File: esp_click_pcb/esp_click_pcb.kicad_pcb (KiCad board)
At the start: 2 copper layers, 90 x 60 mm, 53 parts, among them J1 USB_C, SW1 BOOT, SW2 FLASH, SW3 BT1, SW4 BT2, SW5 BT3, SW6 BT4, U1 ESP32-C6-MINI, U2 HT7833, U4 BQ24075

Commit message: pcb layout complete
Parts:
- D1, D2, D3: footprint LED_SMD:LED_0201_0603Metric -> LED_SMD:LED_0603_1608Metric
- U4: value BQ24075 -> BQ24075RGT
- moved R16 162.6 mm to (183.0, 127.0)
- moved R4 153.1 mm to (172.0, 122.4), turned to 180 degrees
- moved R15 145.7 mm to (161.0, 127.0)
- moved R2 132.7 mm to (148.8, 116.9), turned to 90 degrees
- moved R5 131.7 mm to (151.2, 116.9), turned to 90 degrees
- moved R14 123.8 mm to (139.0, 127.0)
- moved R1 121.5 mm to (128.0, 122.4), turned to 180 degrees
- moved R13 109.1 mm to (117.0, 127.0)
- moved R11 102.3 mm to (130.7, 96.5)
- moved R18 100.7 mm to (117.6, 113.6)
- moved R10 99.8 mm to (126.5, 96.5)
- moved R17 99.3 mm to (113.8, 113.6), turned to 180 degrees
- moved R19 95.5 mm to (120.4, 104.5), turned to 90 degrees
- moved R3 91.9 mm to (124.0, 81.0), turned to 180 degrees
- moved C3 12.1 mm to (107.6, 93.2), turned to 180 degrees
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
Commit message: layout finished pcb
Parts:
- moved SW2 0.10 mm to (172.0, 127.5)
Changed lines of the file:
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@@
 	(footprint "TS-A002:TST-A002_0.6MM_BOSS"
 		(layer "F.Cu")
-		(at 128 127.5 180)
+		(at 128 127.55 180)
 		(property "Reference" "SW1"
 			(at 1 3 0)
@@
 	(footprint "TS-A002:TST-A002_0.6MM_BOSS"
 		(layer "F.Cu")
-		(at 172 127.45 180)
+		(at 172 127.55 180)
 		(property "Reference" "SW2"
 			(at 1 3 0)

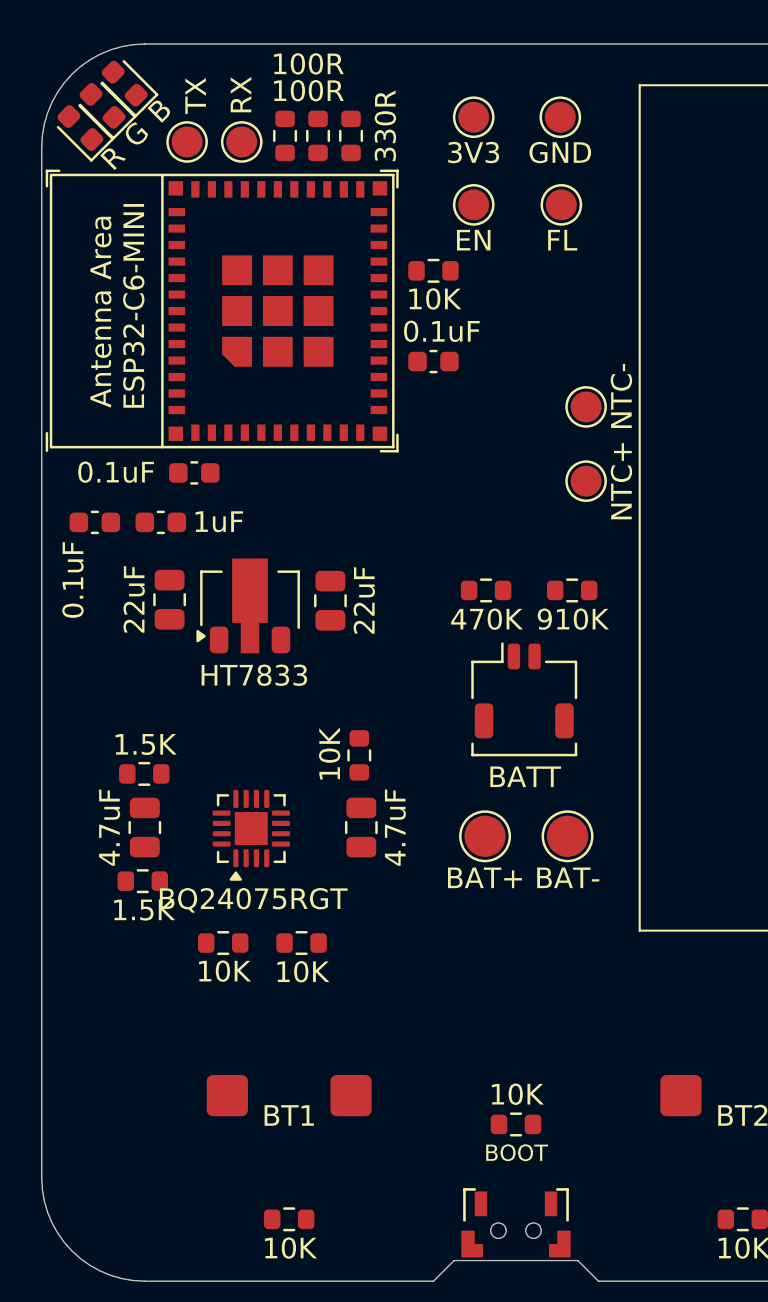
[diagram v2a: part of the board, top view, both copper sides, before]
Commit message: use rgb led directly
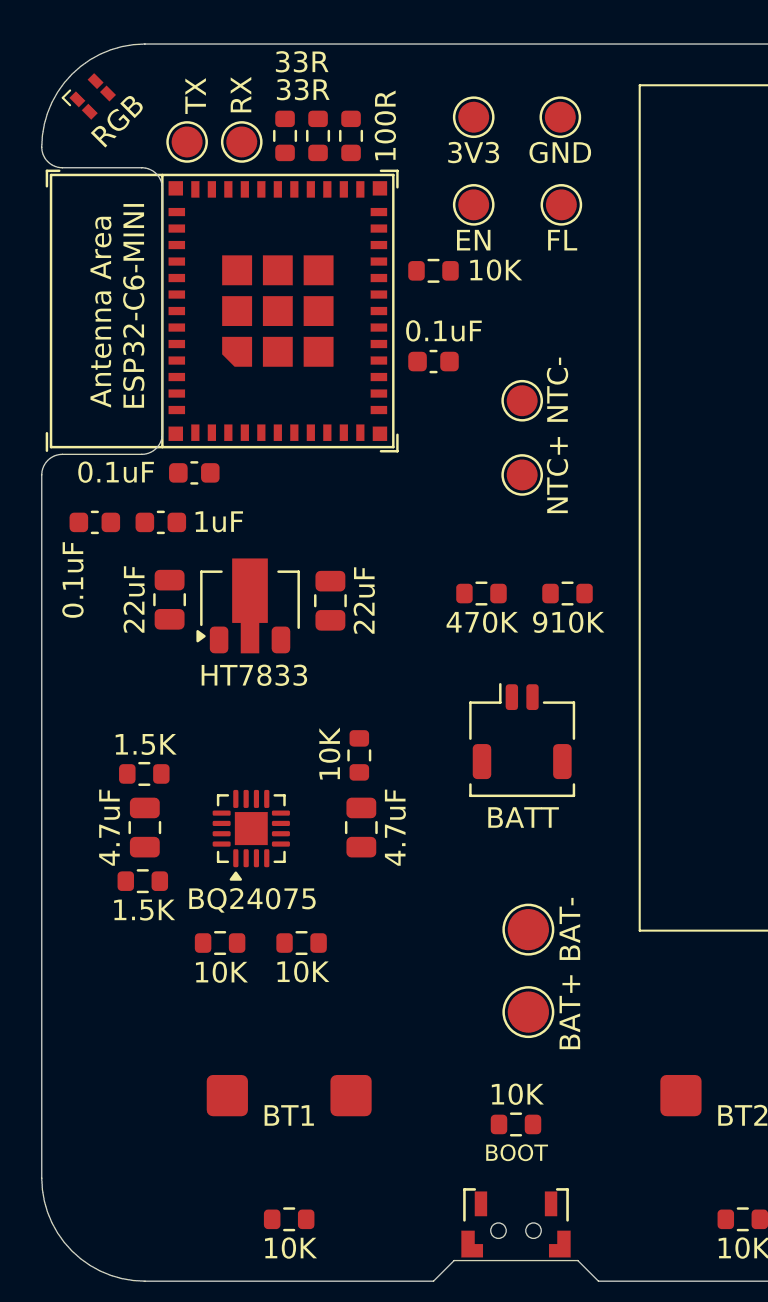
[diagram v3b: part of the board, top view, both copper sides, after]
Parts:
- removed D1: R, LED_SMD:LED_0603_1608Metric
- removed D2: G, LED_SMD:LED_0603_1608Metric
- removed D3: B, LED_SMD:LED_0603_1608Metric
- added LED1: RGB, XL-1615RGBC-RF:XL-1615RGBC-RF, F.Cu at (107.5, 72.5)
- R12, R21: value 100R -> 33R
- R20: value 330R -> 100R
- U4: value BQ24075RGT -> BQ24075
- moved TP7 8.78 mm to (128.6, 117.0), turned to 90 degrees
- moved TP8 4.91 mm to (128.6, 113.0), turned to 90 degrees
- moved TP10 3.11 mm to (128.3, 87.3)
- moved TP9 3.11 mm to (128.3, 90.9)
- moved BATT1 1.98 mm to (128.3, 103.3)
- moved R10 0.27 mm to (126.3, 96.7)
- moved R11 0.27 mm to (130.5, 96.7)
- moved R17 0.15 mm to (113.7, 113.6)
- turned R3 to 0 degrees
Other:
- outline, holes or cut-outs redrawn

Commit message: complete pcb design
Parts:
- moved C3 9.80 mm to (117.3, 92.2)
- moved C5 9.80 mm to (120.5, 92.2), turned to 0 degrees
- moved R2 3.20 mm to (152.0, 116.8)
- moved R5 3.20 mm to (148.0, 116.8)
- moved TP7 0.81 mm to (128.0, 117.5)
- moved TP8 0.81 mm to (128.0, 113.5)
- moved TP6 0.18 mm to (114.6, 74.6)
- moved TP5 0.18 mm to (112.0, 74.6)
- turned R12 to -90 degrees
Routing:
- net +3.3V: track 0.00 -> 197.2 mm, vias 0 -> 7
- net Net-(U1-EN/CHIP_PU): track 0.00 -> 109.3 mm, vias 0 -> 7
- net Net-(U1-GPIO9): track 0.00 -> 106.1 mm, vias 0 -> 4
- net B4: track 0.00 -> 99.3 mm, vias 0 -> 4
- net B3: track 0.00 -> 77.9 mm, vias 0 -> 4
- net +5V: track 0.00 -> 69.3 mm
- net B1: track 0.00 -> 63.6 mm, vias 0 -> 6
- net B2: track 0.00 -> 60.7 mm, vias 0 -> 6
- net Net-(U1-GPIO13/USB_D+): track 0.00 -> 59.7 mm
- net Net-(U1-GPIO12/USB_D-): track 0.00 -> 59.4 mm
- net GND: track 0.00 -> 42.9 mm, vias 0 -> 81
- net Net-(U4-TS): track 0.00 -> 42.7 mm, vias 0 -> 2
- net BATT+: track 0.00 -> 41.4 mm
- net CHG: track 0.00 -> 36.1 mm, vias 0 -> 2
- net PGOOD: track 0.00 -> 35.0 mm, vias 0 -> 4
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- added copper zone on B.Cu, net GND
- added copper zone on F.Cu, net GND
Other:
- outline, holes or cut-outs redrawn

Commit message: production build
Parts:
- added G***: LOGO, LOGO, F.Cu at (165.0, 87.0)
- added G***: LOGO, LOGO, B.Cu at (150.0, 94.0)
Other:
- board text added: "ESP CLICK"
- board text added: "JLCJLCJLCJLC"
- board text added: "REV 1 - 2026 MADHUKAR TEMBA"

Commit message: update pcb design, rev2
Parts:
- removed R4: 10K, Resistor_SMD:R_0603_1608Metric
- R12, R21: value 33R -> 100R
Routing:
- net +3.3V: track 197.2 -> 194.0 mm
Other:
- board text added: "REV 2 - 2026 MADHUKAR TEMBA"
- board text removed: "REV 1 - 2026 MADHUKAR TEMBA"
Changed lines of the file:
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@@
 	(title_block
 		(title "ESP Click")
-		(date "2026-03-06")
-		(rev "1")
+		(date "2026-03-13")
+		(rev "2")
 		(company "Madhukar Temba")
 	)
@@
 			)
 		)
-		(property "Value" "33R"
+		(property "Value" "100R"
 			(at -3.555 -0.8 180)
 			(layer "F.SilkS")
@@
 		(embedded_fonts no)
 	)
-	(footprint "Resistor_SMD:R_0603_1608Metric"
-		(layer "F.Cu")
-		(at 172 122.4 180)
-		(descr "Resistor SMD 0603 (1608 Metric), square (rectangular) end terminal, IPC-7351 nominal, (Body size source: IPC-SM-782 page 72, https://www.pcb-3d.com/wordpress/wp-content/uploads/ipc-sm-782a_amendment_1_and_2.pdf), generated with kicad-footprint-generator")
-		(tags "resistor")
-		(property "Reference" "R4"
-			(at 0 -1.43 0)
-			(layer "User.4")
-			(effects
-				(font
-					(size 1 1)
-					(thickness 0.15)
-				)
-			)
-		)
-		(property "Value" "10K"
-			(at 0 1.43 0)
-			(layer "F.SilkS")
-			(effects
-				(font
-					(size 1 1)
-					(thickness 0.15)
-				)
-			)
-		)
-		(property "Datasheet" "~"
-			(at 0 0 0)
-			(layer "F.Fab")
-			(hide yes)
-			(effects
-				(font
-					(size 1.27 1.27)
-					(thickness 0.15)
-				)
-			)
-		)
-		(property "Description" "Resistor"
-			(at 0 0 0)
-			(layer "F.Fab")
-			(hide yes)
-			(effects
-				(font
-					(size 1.27 1.27)
-					(thickness 0.15)
-				)
-			)
-		)
-		(property ki_fp_filters "R_*")
-		(sheetname "/")
-		(sheetfile "esp_click_pcb.kicad_sch")
-		(attr smd)
-		(fp_line
-			(start -0.237258 0.5225)
-			(end 0.237258 0.5225)
-			(stroke
-				(width 0.12)
-				(type solid)
-			)
-			(layer "F.SilkS")
-		)
-		(fp_line
-			(start -0.237258 -0.5225)
-			(end 0.237258 -0.5225)
-			(stroke
-				(width 0.12)
-				(type solid)
-			)
-			(layer "F.SilkS")
-		)
-		(fp_rect
-			(start -1.48 -0.73)
-			(end 1.48 0.73)
-			(stroke
-				(width 0.05)
-				(type solid)
-			)
-			(fill no)
-			(layer "F.CrtYd")
-		)
-		(fp_rect
-			(start -0.8 -0.4125)
-			(end 0.8 0.4125)
-			(stroke
-				(width 0.1)
-				(type solid)
-			)
-			(fill no)
-			(layer "F.Fab")
-		)
-		(fp_text user "${REFERENCE}"
-			(at 0 0 0)
-			(layer "User.4")
-			(effects
-				(font
-					(size 0.4 0.4)
-					(thickness 0.06)
-				)
-			)
-		)
-		(pad "1" smd roundrect
-			(at -0.825 0 180)
-			(size 0.8 0.95)
-			(layers "F.Cu" "F.Mask" "F.Paste")
-			(roundrect_rratio 0.25)
-			(net 16 "Net-(U1-GPIO9)")
-			(pintype "passive")
-		)
-		(pad "2" smd roundrect
-			(at 0.825 0 180)
-			(size 0.8 0.95)
-			(layers "F.Cu" "F.Mask" "F.Paste")
-			(roundrect_rratio 0.25)
-			(net 3 "+3.3V")
-			(pintype "passive")
-		)
-		(embedded_fonts no)
-		(model "${KICAD9_3DMODEL_DIR}/Resistor_SMD.3dshapes/R_0603_1608Metric.step"
-			(offset
-				(xyz 0 0 0)
-			)
-			(scale
-				(xyz 1 1 1)
-			)
-			(rotate
-				(xyz 0 0 0)
-			)
-		)
-	)
 	(footprint "TestPoint:TestPoint_Pad_D1.5mm"
 		(layer "F.Cu")
@@
 			)
 		)
-		(property "Value" "33R"
+		(property "Value" "100R"
 			(at -2.155 0.8 0)
 			(layer "F.SilkS")
@@
 		)
 	)
-	(gr_text "REV 1 - 2026\nMADHUKAR TEMBA"
+	(gr_text "REV 2 - 2026\nMADHUKAR TEMBA"
 		(at 189 125 0)
 		(layer "B.SilkS")
@@
 			(justify left bottom mirror)
 		)
-		(render_cache "REV 1 - 2026\nMADHUKAR TEMBA" 0
+		(render_cache "REV 2 - 2026\nMADHUKAR TEMBA" 0
 			(polygon
 				(pts
@@
 			(polygon
 				(pts
-					(xy 178.644347 119.45) (xy 178.644347 117.271598) (xy 179.19829 117.699694) (xy 179.563555 117.20034)
-					(xy 178.585546 116.483914) (xy 177.939279 116.483914) (xy 177.939279 119.45)
+					(xy 179.546702 119.45) (xy 179.546702 118.865465) (xy 178.388258 117.82151) (xy 178.287825 117.71381)
+					(xy 178.212037 117.608653) (xy 178.161801 117.494462) (xy 178.144809 117.366486) (xy 178.156618 117.264867)
+					(xy 178.190265 117.180568) (xy 178.24556 117.109665) (xy 178.318151 117.056213) (xy 178.406267 117.023193)
+					(xy 178.514288 117.011479) (xy 178.626245 117.025697) (xy 178.72064 117.066697) (xy 178.8017 117.13531)
+					(xy 178.864203 117.223546) (xy 178.908625 117.330616) (xy 178.933958 117.460642) (xy 179.609717 117.368318)
+					(xy 179.56525 117.151029) (xy 179.485886 116.963668) (xy 179.373564 116.798017) (xy 179.236209 116.659769)
+					(xy 179.075058 116.549434) (xy 178.889994 116.467978) (xy 178.69039 116.418612) (xy 178.476369 116.401849)
+					(xy 178.273377 116.415575) (xy 178.077765 116.456437) (xy 177.893922 116.52634) (xy 177.733565 116.624415)
+					(xy 177.598115 116.751866) (xy 177.492315 116.909813) (xy 177.443216 117.027631) (xy 177.412671 117.160941)
+					(xy 177.402006 117.31263) (xy 177.412944 117.467361) (xy 177.443954 117.600226) (xy 177.493935 117.723735)
+					(xy 177.559359 117.837264) (xy 177.637924 117.942586) (xy 177.727337 118.040963) (xy 177.922426 118.227625)
+					(xy 178.610825 118.840369) (xy 177.397793 118.840369) (xy 177.397793 119.45)
 				)
 			)
@@
 	)
 	(segment
-		(start 175.25 123.75)
-		(end 176.75 125.25)
-		(width 0.4)
-		(layer "F.Cu")
-		(net 3)
-	)
-	(segment
 		(start 114.25 91.25)
 		(end 113.625 91.25)
@@
 	)
 	(segment
-		(start 183.825 126.325)
-		(end 183.825 127)
-		(width 0.4)
-		(layer "F.Cu")
-		(net 3)
-	)
-	(segment
 		(start 118 125.75)
 		(end 117.825 125.925)
@@
 	)
 	(segment
-		(start 176.75 125.25)
-		(end 182.75 125.25)
-		(width 0.4)
-		(layer "F.Cu")
-		(net 3)
-	)
-	(segment
 		(start 117.675 103.675)
 		(end 120.4 103.675)
@@
 	)
 	(segment
-		(start 182.75 125.25)
-		(end 183.825 126.325)
-		(width 0.4)
-		(layer "F.Cu")
-		(net 3)
-	)
-	(segment
 		(start 115 94)
 		(end 119.75 94)
@@
 	)
 	(segment
-		(start 119.875 103.675)
-		(end 120.4 103.675)
+		(start 161.825 127)
+		(end 166 127)
 		(width 0.4)
 		(layer "F.Cu")
@@
 	)
 	(segment
-		(start 167.25 125.75)
-		(end 167.25 123)
+		(start 119.875 103.675)
+		(end 120.4 103.675)
 		(width 0.4)
 		(layer "F.Cu")
@@
 	)
 	(segment
+		(start 175.25 123.75)
+		(end 176.75 125.25)
+		(width 0.4)
+		(layer "F.Cu")
+		(net 3)
+	)
+	(segment
 		(start 117.825 125.925)
 		(end 117.825 127)
@@
 	)
 	(segment
+		(start 169.25 123.75)
+		(end 175.25 123.75)
+		(width 0.4)
+		(layer "F.Cu")
+		(net 3)
+	)
+	(segment
 		(start 113.175 90.8)
 		(end 113.175 92.175)
@@
 	)
 	(segment
+		(start 166 127)
+		(end 169.25 123.75)
+		(width 0.4)
+		(layer "F.Cu")
+		(net 3)
+	)
+	(segment
 		(start 114.625 90.875)
 		(end 114.25 91.25)
@@
 	)
 	(segment
-		(start 167.25 123)
-		(end 167.85 122.4)
-		(width 0.4)
-		(layer "F.Cu")
-		(net 3)
-	)
-	(segment
 		(start 127.175 122.4)
 		(end 127.175 122.925)
@@
 	)
 	(segment
-		(start 171.175 122.4)
-		(end 171.175 123.175)
-		(width 0.4)
-		(layer "F.Cu")
-		(net 3)
-	)
-	(segment
 		(start 118.9 104.65)
 		(end 119.875 103.675)
@@
 	)
 	(segment
-		(start 167.85 122.4)
-		(end 171.175 122.4)
-		(width 0.4)
-		(layer "F.Cu")
-		(net 3)
-	)
-	(segment
 		(start 118.425 112.375)
 		(end 118.45 112.35)
@@
 	)
 	(segment
-		(start 171.75 123.75)
-		(end 175.25 123.75)
-		(width 0.4)
-		(layer "F.Cu")
-		(net 3)
-	)
-	(segment
 		(start 121.25 97)
 		(end 120.3 97.95)
@@
 	)
 	(segment
-		(start 166 127)
-		(end 167.25 125.75)
+		(start 183.825 126.325)
+		(end 183.825 127)
 		(width 0.4)
 		(layer "F.Cu")
@@
 	)
 	(segment
-		(start 125.95 73.55)
-		(end 123.55 73.55)
-		(width 0.3)
+		(start 176.75 125.25)
+		(end 182.75 125.25)
+		(width 0.4)
 		(layer "F.Cu")
 		(net 3)
 	)
 	(segment
-		(start 161.825 127)
-		(end 166 127)
-		(width 0.4)
+		(start 125.95 73.55)
+		(end 123.55 73.55)
+		(width 0.3)
 		(layer "F.Cu")
 		(net 3)
@@
 	)
 	(segment
-		(start 171.175 123.175)
-		(end 171.75 123.75)
+		(start 182.75 125.25)
+		(end 183.825 126.325)
 		(width 0.4)
 		(layer "F.Cu")
@@
 	)
 	(segment
+		(start 174 122.75)
+		(end 173.575 122.75)
+		(width 0.3)
+		(layer "F.Cu")
+		(net 16)
+	)
+	(segment
 		(start 128.5 82.2)
 		(end 126.9 82.2)
@@
 	)
 	(segment
-		(start 173.65 122.4)
-		(end 174 122.75)
-		(width 0.4)
+		(start 173.575 122.75)
+		(end 172.825 122)
+		(width 0.3)
 		(layer "F.Cu")
 		(net 16)
@@
 	)
 	(segment
-		(start 172.825 122.4)
-		(end 173.65 122.4)
-		(width 0.4)
-		(layer "F.Cu")
-		(net 16)
-	)
-	(segment
 		(start 130.2 77.8)
 		(end 130.2 80.5)
@@
 	)
 	(segment
-		(start 172.825 122.4)
+		(start 172.825 122)
 		(end 172.825 83.325)
 		(width 0.3)

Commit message: rev 3
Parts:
- R9: value 1.5K -> 3K
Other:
- board text added: "REV 3 - 2026 MADHUKAR TEMBA"
- board text removed: "REV 2 - 2026 MADHUKAR TEMBA"
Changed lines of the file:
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@@
 	(title_block
 		(title "ESP Click")
-		(date "2026-03-13")
-		(rev "2")
+		(date "2026-03-14")
+		(rev "3")
 		(company "Madhukar Temba")
 	)
@@
 			)
 		)
-		(property "Value" "1.5K"
+		(property "Value" "3K"
 			(at 0 1.43 0)
 			(layer "F.SilkS")
@@
 		)
 	)
-	(gr_text "REV 2 - 2026\nMADHUKAR TEMBA"
+	(gr_text "REV 3 - 2026\nMADHUKAR TEMBA"
 		(at 189 125 0)
 		(layer "B.SilkS")
@@
 			(justify left bottom mirror)
 		)
-		(render_cache "REV 2 - 2026\nMADHUKAR TEMBA" 0
+		(render_cache "REV 3 - 2026\nMADHUKAR TEMBA" 0
 			(polygon
 				(pts
@@
 			(polygon
 				(pts
-					(xy 179.546702 119.45) (xy 179.546702 118.865465) (xy 178.388258 117.82151) (xy 178.287825 117.71381)
-					(xy 178.212037 117.608653) (xy 178.161801 117.494462) (xy 178.144809 117.366486) (xy 178.156618 117.264867)
-					(xy 178.190265 117.180568) (xy 178.24556 117.109665) (xy 178.318151 117.056213) (xy 178.406267 117.023193)
-					(xy 178.514288 117.011479) (xy 178.626245 117.025697) (xy 178.72064 117.066697) (xy 178.8017 117.13531)
-					(xy 178.864203 117.223546) (xy 178.908625 117.330616) (xy 178.933958 117.460642) (xy 179.609717 117.368318)
-					(xy 179.56525 117.151029) (xy 179.485886 116.963668) (xy 179.373564 116.798017) (xy 179.236209 116.659769)
-					(xy 179.075058 116.549434) (xy 178.889994 116.467978) (xy 178.69039 116.418612) (xy 178.476369 116.401849)
-					(xy 178.273377 116.415575) (xy 178.077765 116.456437) (xy 177.893922 116.52634) (xy 177.733565 116.624415)
-					(xy 177.598115 116.751866) (xy 177.492315 116.909813) (xy 177.443216 117.027631) (xy 177.412671 117.160941)
-					(xy 177.402006 117.31263) (xy 177.412944 117.467361) (xy 177.443954 117.600226) (xy 177.493935 117.723735)
-					(xy 177.559359 117.837264) (xy 177.637924 117.942586) (xy 177.727337 118.040963) (xy 177.922426 118.227625)
-					(xy 178.610825 118.840369) (xy 177.397793 118.840369) (xy 177.397793 119.45)
+					(xy 177.385153 118.587761) (xy 177.396837 118.747561) (xy 177.430238 118.887084) (xy 177.483888 119.00963)
+					(xy 177.598221 119.172761) (xy 177.741992 119.303271) (xy 177.91025 119.403428) (xy 178.100846 119.475279)
+					(xy 178.301929 119.517894) (xy 178.505861 119.532065) (xy 178.705346 119.520547) (xy 178.898421 119.48627)
+					(xy 179.082382 119.428072) (xy 179.24665 119.347051) (xy 179.393572 119.240414) (xy 179.521606 119.105983)
+					(xy 179.622793 118.946) (xy 179.697827 118.748595) (xy 179.043135 118.576404) (xy 178.980241 118.712593)
+					(xy 178.870943 118.834691) (xy 178.778673 118.895312) (xy 178.669626 118.93271) (xy 178.539384 118.945882)
+					(xy 178.386243 118.924816) (xy 178.312218 118.897527) (xy 178.247758 118.859237) (xy 178.192585 118.808494)
+					(xy 178.147008 118.742916) (xy 178.11771 118.665482) (xy 178.107074 118.565413) (xy 178.120938 118.458112)
+					(xy 178.159647 118.375087) (xy 178.220072 118.307193) (xy 178.298133 118.254553) (xy 178.388205 118.217083)
+					(xy 178.493222 118.191172) (xy 178.711392 118.172121) (xy 178.900436 118.172121) (xy 178.900436 117.65628)
+					(xy 178.694722 117.65628) (xy 178.501648 117.641625) (xy 178.412905 117.620275) (xy 178.335868 117.587037)
+					(xy 178.269483 117.54005) (xy 178.218449 117.480059) (xy 178.186228 117.405812) (xy 178.174302 117.303654)
+					(xy 178.187669 117.203115) (xy 178.225371 117.123738) (xy 178.287691 117.060389) (xy 178.408656 116.997545)
+					(xy 178.54781 116.976308) (xy 178.645343 116.986611) (xy 178.731955 117.016635) (xy 178.810127 117.066617)
+					(xy 178.87511 117.132814) (xy 178.923174 117.212386) (xy 178.954841 117.307868) (xy 179.609717 117.156742)
+					(xy 179.54047 116.97799) (xy 179.445952 116.827564) (xy 179.326694 116.698473) (xy 179.187848 116.592725)
+					(xy 179.032784 116.51009) (xy 178.8627 116.450026) (xy 178.684445 116.413921) (xy 178.501648 116.401849)
+					(xy 178.306552 116.414504) (xy 178.117698 116.452224) (xy 177.93943 116.516902) (xy 177.783941 116.607562)
+					(xy 177.651296 116.725408) (xy 177.546903 116.869696) (xy 177.497747 116.977838) (xy 177.467244 117.100572)
+					(xy 177.456594 117.240823) (xy 177.472984 117.40084) (xy 177.520068 117.53849) (xy 177.597278 117.658478)
+					(xy 177.699504 117.759274) (xy 177.818162 117.834989) (xy 177.955949 117.886906) (xy 177.955949 117.899546)
+					(xy 177.834701 117.938086) (xy 177.725139 117.994068) (xy 177.627026 118.065868) (xy 177.544705 118.149406)
+					(xy 177.477547 118.244678) (xy 177.427102 118.350724) (xy 177.395786 118.464755)
 				)
 			)
